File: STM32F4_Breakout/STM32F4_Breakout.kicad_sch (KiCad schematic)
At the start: 1 part

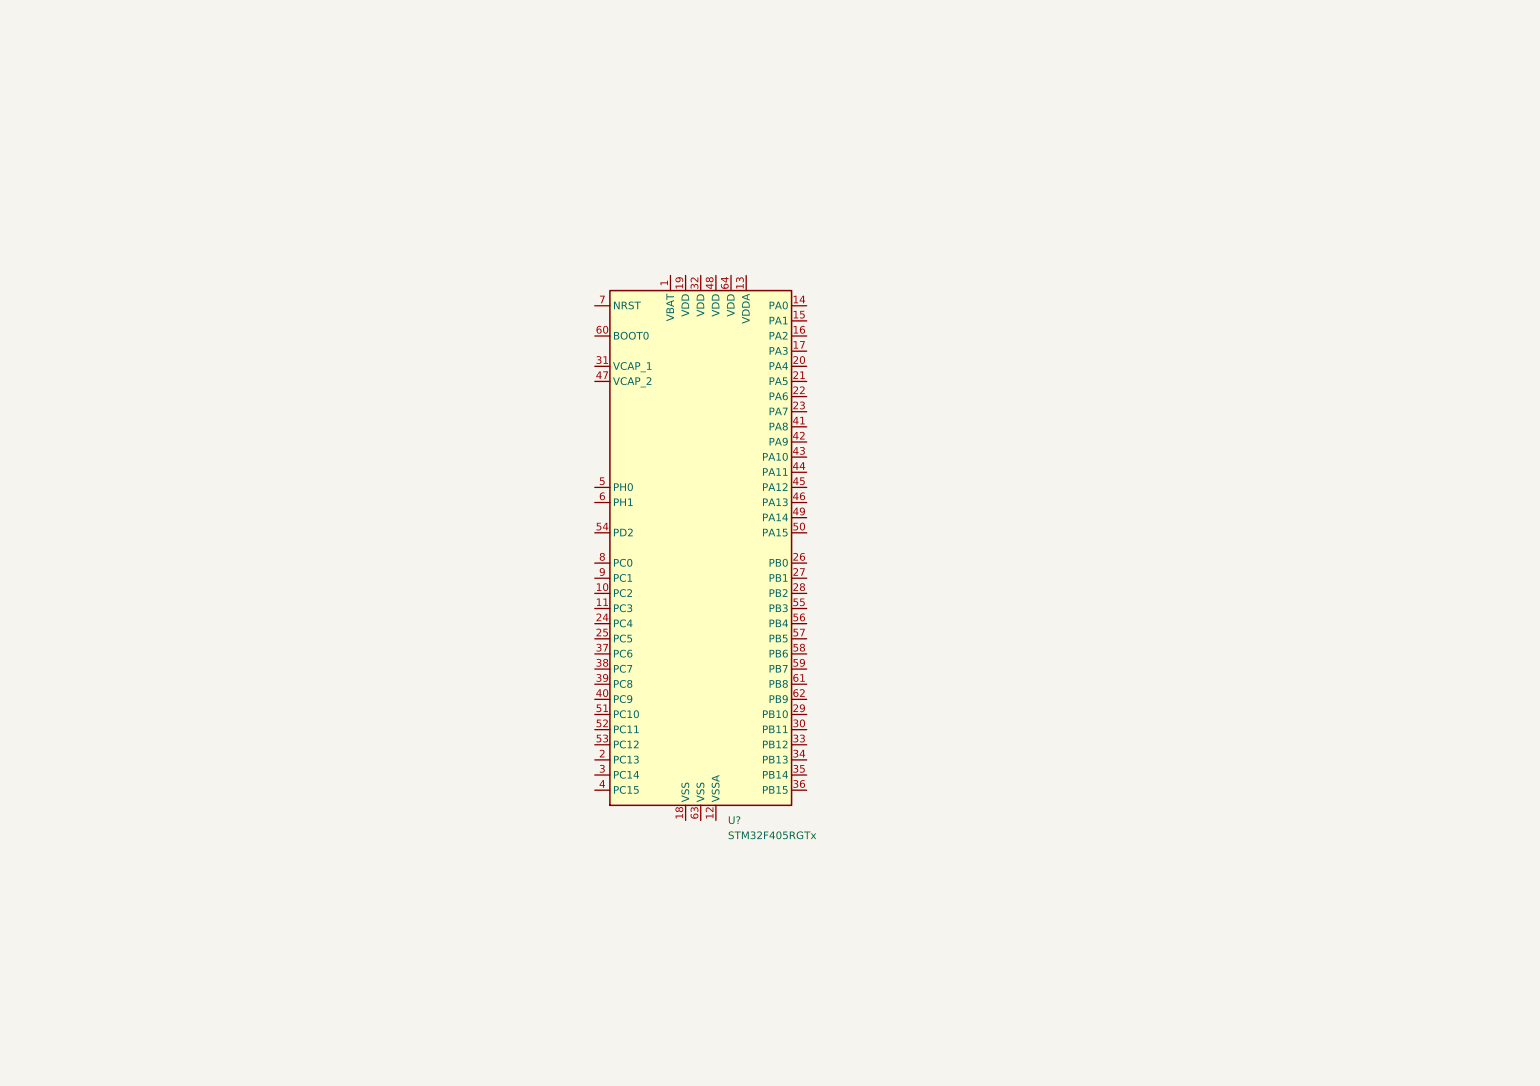
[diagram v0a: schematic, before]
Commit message: Setting up power supply (regulation, protection, filtering)
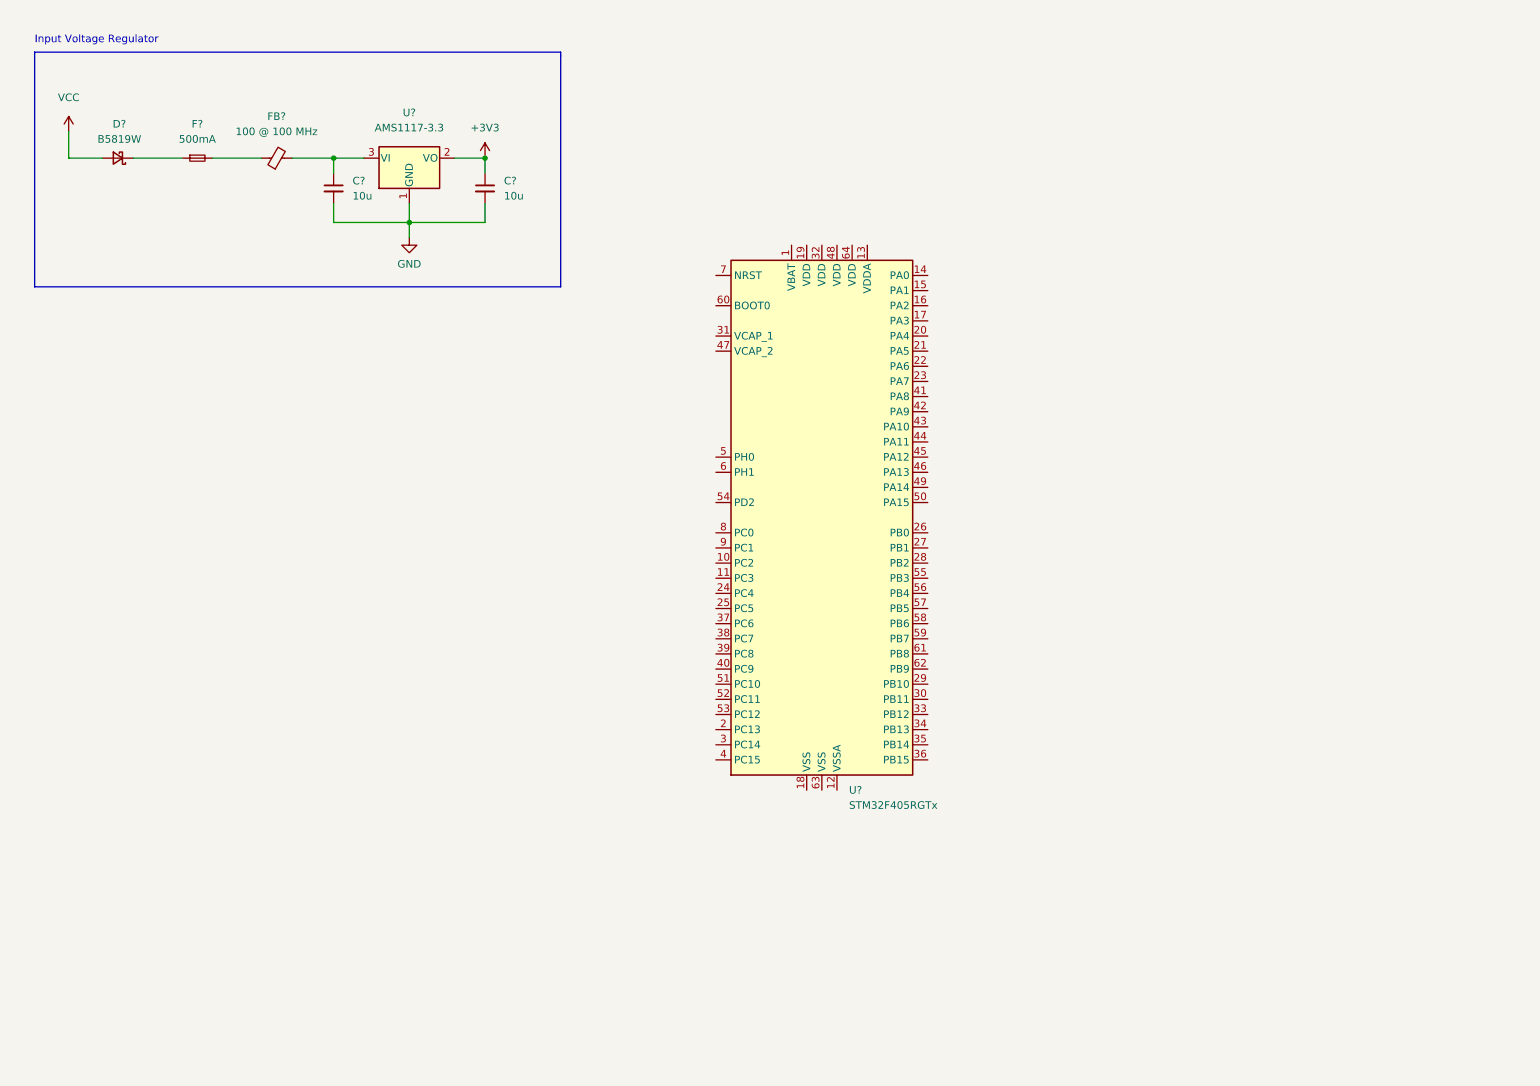
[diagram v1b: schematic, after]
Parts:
- added C? (x2): 10u, symbol Device:C_Small
- added D?: B5819W, symbol Device:D_Schottky_Small
- added F?: 500mA, symbol Device:Fuse_Small
- added FB?: 100 @ 100 MHz, symbol Device:FerriteBead_Small
- added U?: AMS1117-3.3, Package_TO_SOT_SMD:SOT-223-3_TabPin2, symbol Regulator_Linear:AMS1117-3.3
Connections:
- new net: F?.2, FB?.1
- new net: C?.1, FB?.2, U?.3 (VI)
- new net: D?.1 (K), F?.1
- new net +3V3: C?.1, U?.2 (VO)
- new net GND: C?.2, C?.2, U?.1 (GND)
- new net VCC: D?.2 (A)
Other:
- note added: "Input Voltage Regulator"
- moved on the sheet: U?

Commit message: adding decoupling caps, vdda filtering, bootmodes
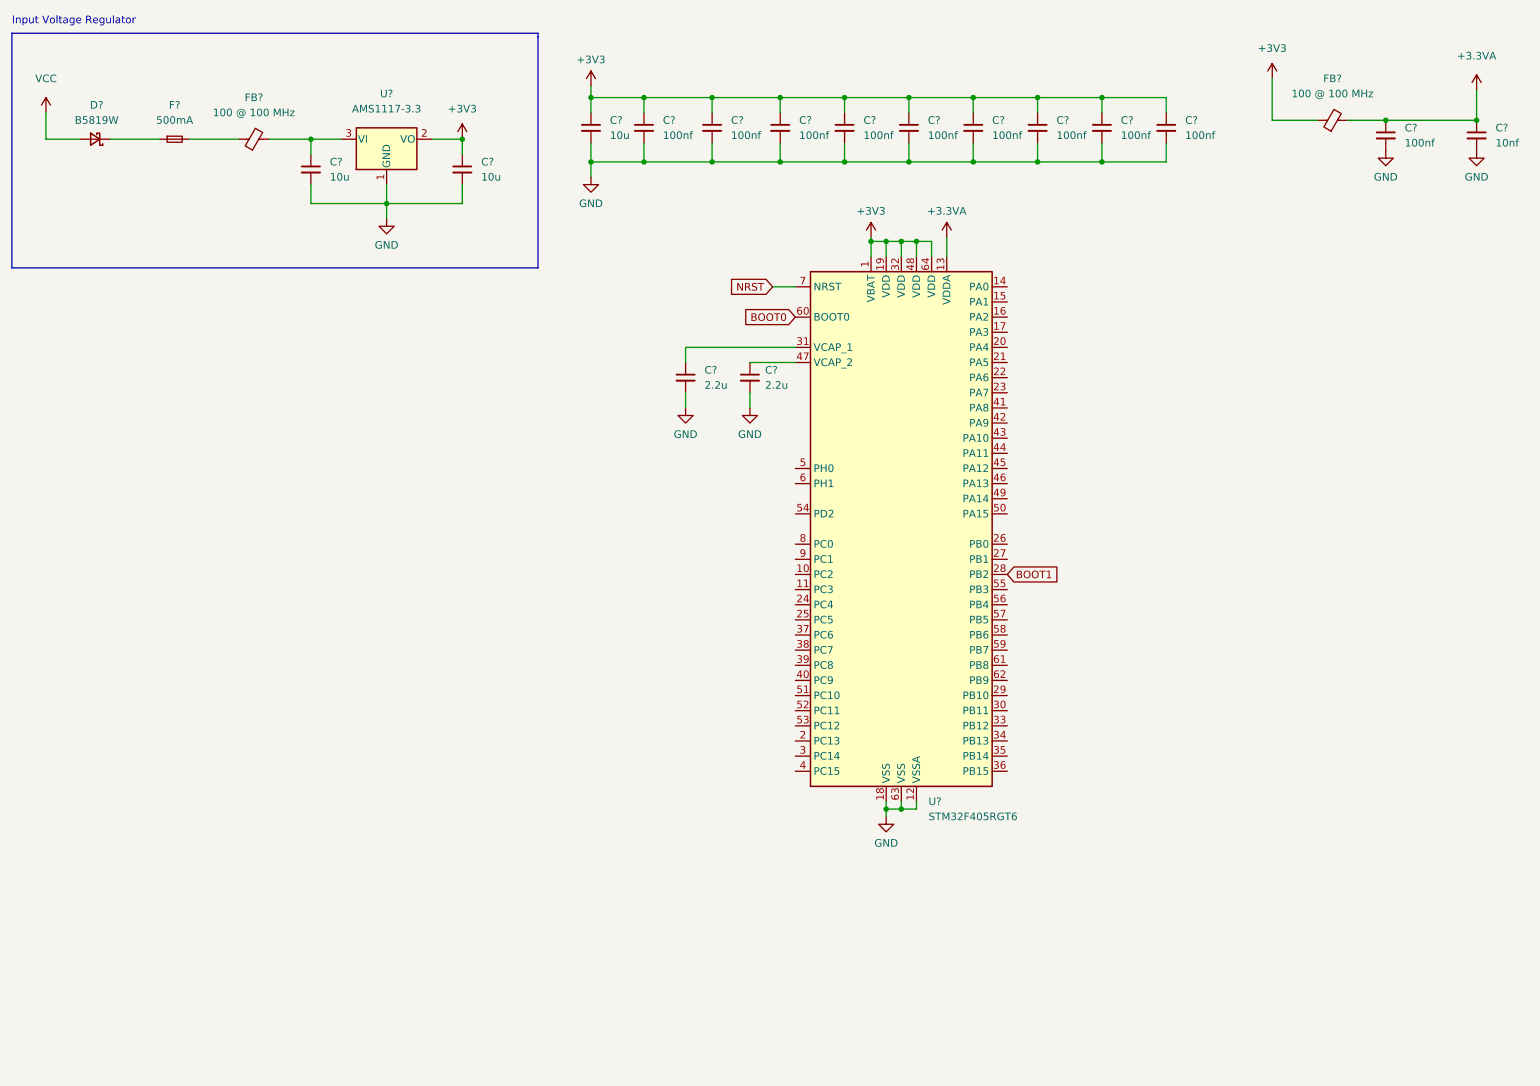
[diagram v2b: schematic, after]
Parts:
- added C? (x10): 100nf, symbol Device:C_Small
- added C? (x2): 2.2u, symbol Device:C_Small
- added C?: 10u, symbol Device:C_Small
- added C?: 10nf, symbol Device:C_Small
- added FB?: 100 @ 100 MHz, symbol Device:FerriteBead_Small
- U?: value STM32F405RGTx -> STM32F405RGT6
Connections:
- net +3V3: now also U?.1 (VBAT), U?.19 (VDD), U?.32 (VDD), U?.48 (VDD), U?.64 (VDD), C?.1, C?.1, C?.1, C?.1, C?.1, C?.1, C?.1, C?.1, C?.1, C?.1, FB?.1
- net GND: now also U?.12 (VSSA), U?.18 (VSS), U?.63 (VSS), C?.2, C?.2, C?.2, C?.2, C?.2, C?.2, C?.2, C?.2, C?.2, C?.2, C?.2, C?.2, C?.2, C?.2
- net +3.3VA: now reaches U?.13 (VDDA)
- net +3.3VA: now also C?.1, C?.1, FB?.2
- net BOOT1: now reaches U?.28 (PB2)
- net at U?.31 (VCAP_1): now also C?.1
- net at U?.47 (VCAP_2): now also C?.1
- net BOOT0: now reaches U?.60 (BOOT0)
- net NRST: now reaches U?.7 (NRST)
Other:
- moved on the sheet: C?, D?, F?, FB?, U?

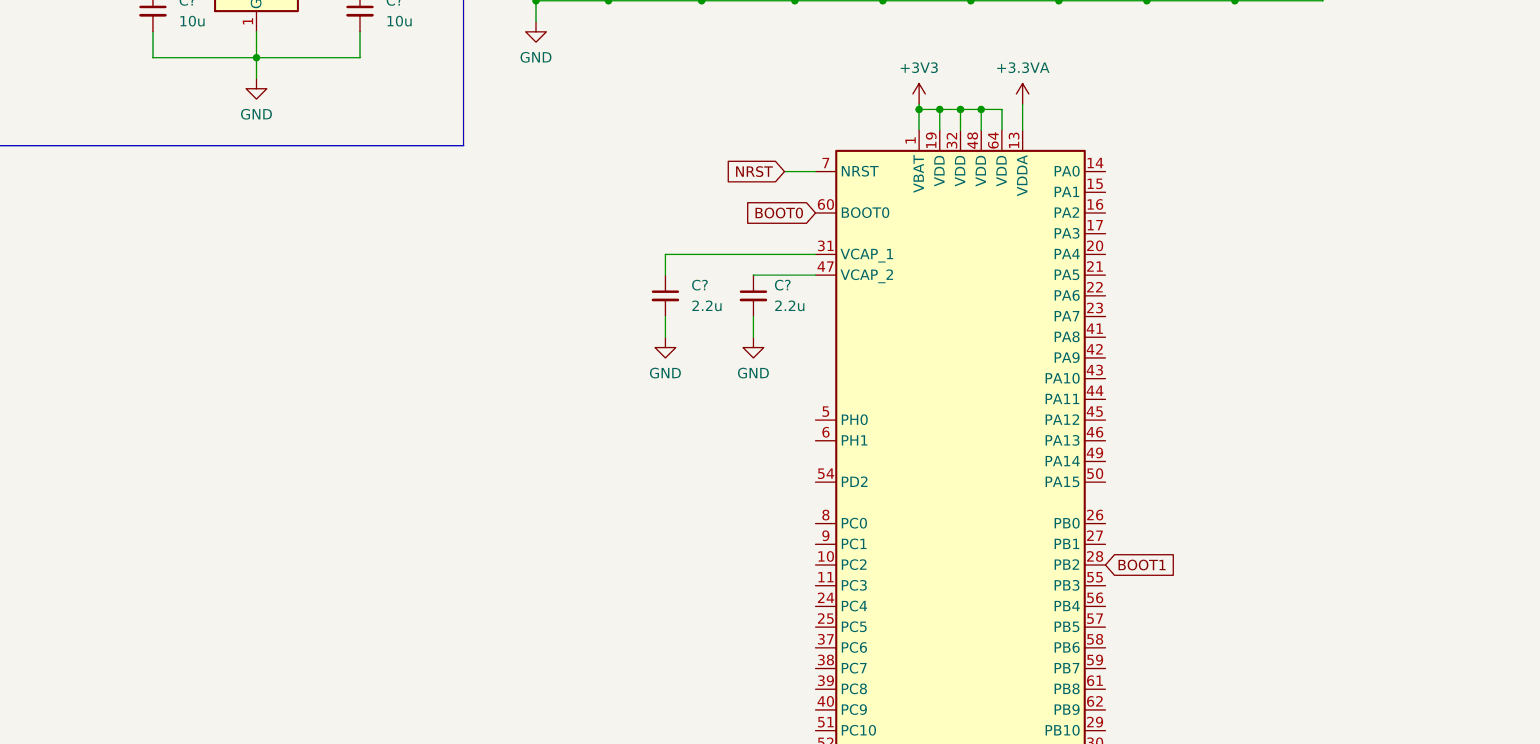
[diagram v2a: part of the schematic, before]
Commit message: crystal oscillator (HSE, Load Capacitors, Feed resistor)
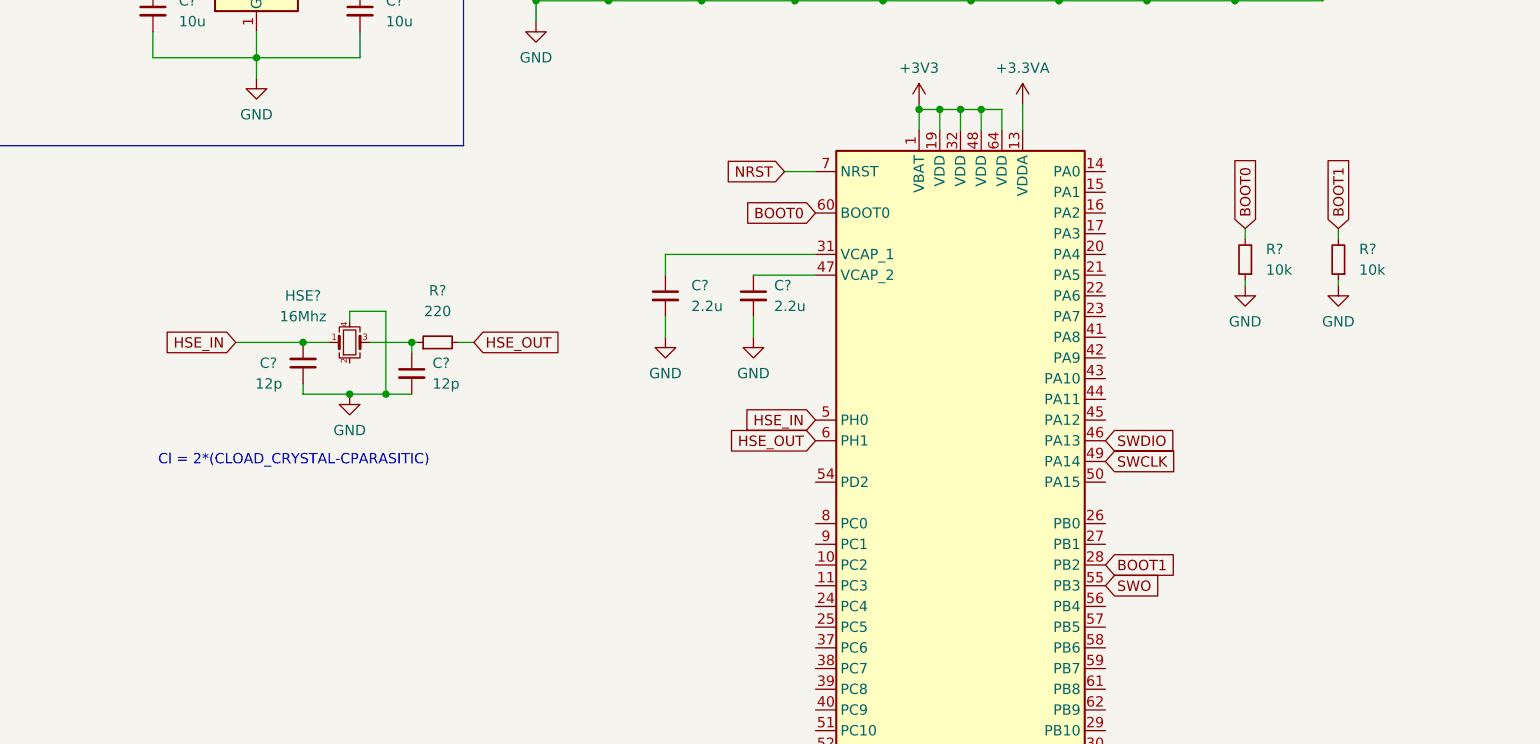
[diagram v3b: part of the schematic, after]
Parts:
- added C? (x2): 12p, symbol Device:C_Small
- added HSE?: 16Mhz, symbol Device:Crystal_GND24_Small
- added R? (x2): 10k, symbol Device:R_Small
- added R?: 220, symbol Device:R_Small
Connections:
- net BOOT0: now also R?.2
- net BOOT1: now also R?.2
- net GND: now also C?.1, C?.2, HSE?.4, R?.1, R?.1
- net SWDIO: now reaches U?.46 (PA13)
- net SWCLK: now reaches U?.49 (PA14)
- net HSE_IN: now reaches U?.5 (PH0)
- net HSE_IN: now also C?.2, HSE?.1
- net SWO: now reaches U?.55 (PB3)
- net HSE_OUT: now reaches U?.6 (PH1)
- net HSE_OUT: now also R?.2
- new net: C?.1, HSE?.3, R?.1
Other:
- note added: "Cl = 2*(CLOAD_CRYSTAL-CPARASITIC)"
